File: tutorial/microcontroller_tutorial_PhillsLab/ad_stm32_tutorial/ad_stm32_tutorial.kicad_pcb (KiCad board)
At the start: 2 copper layers, 41 x 25.8 mm, 34 parts, among them J1 USB_C_Receptacle_USB2.0_16P, J2 TagConnect_TC2030-NL, J3 Conn_01x06, U1 STM32F042G6Ux, Y1 Crystal_GND24

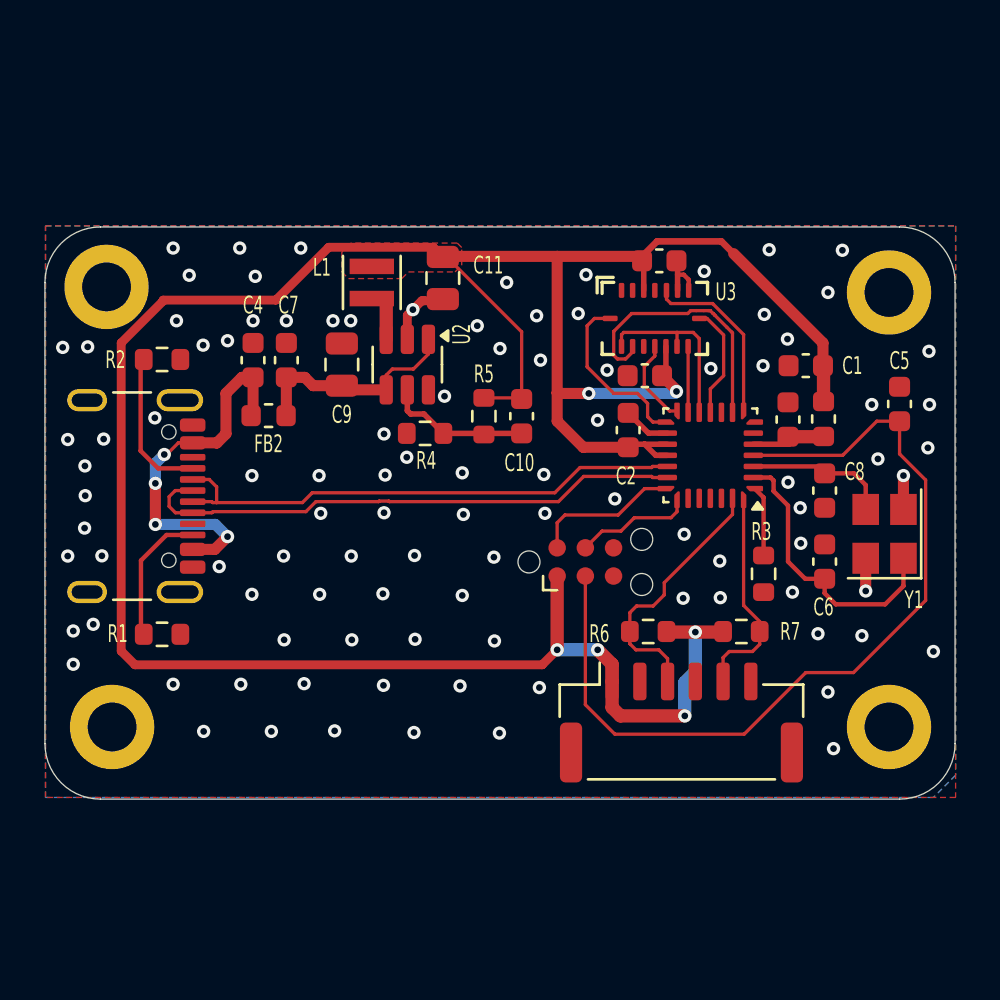
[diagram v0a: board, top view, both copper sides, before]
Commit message: Added all 3d models
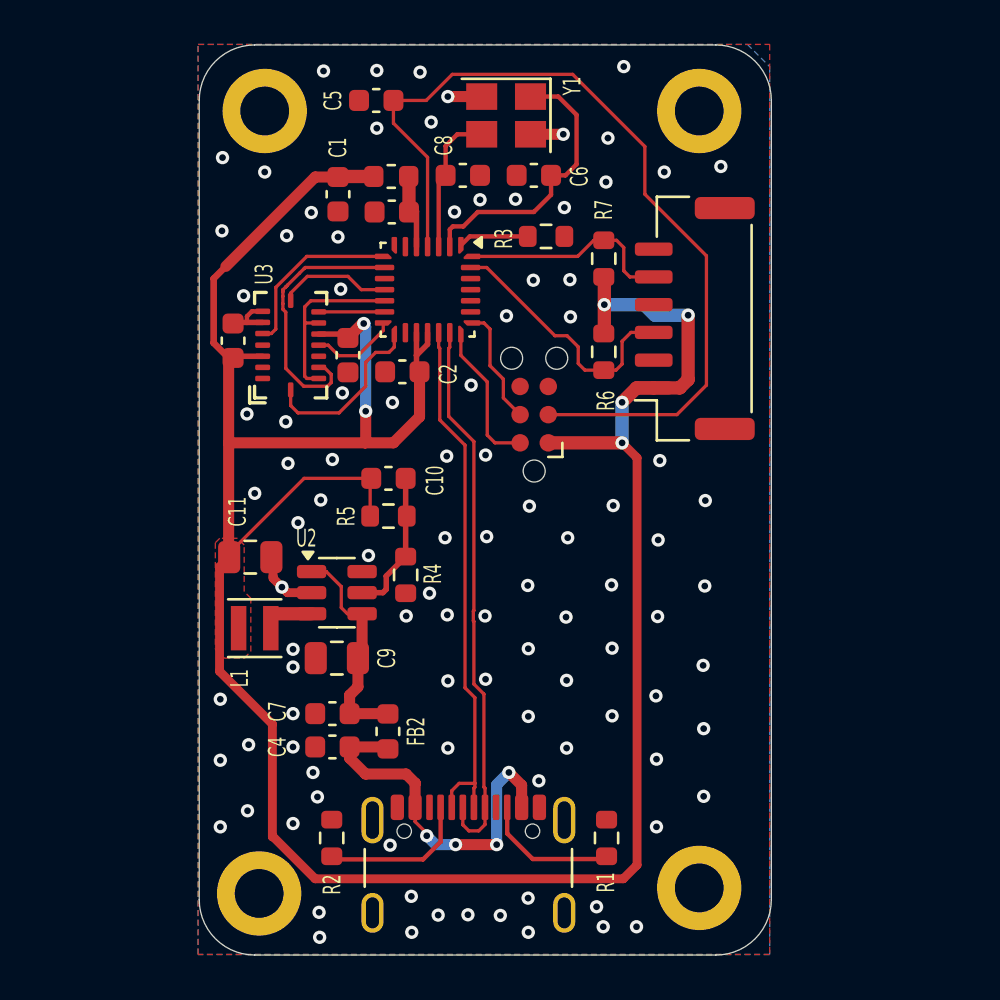
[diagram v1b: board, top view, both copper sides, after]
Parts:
- moved REF** 29.3 mm to (129.1, 70.6), turned to 90 degrees
- moved REF** 29.0 mm to (148.7, 70.6), turned to 90 degrees
- moved REF** 28.2 mm to (128.9, 105.8), turned to 90 degrees
- moved REF** 27.4 mm to (148.7, 105.6), turned to 90 degrees
- moved C5 27.3 mm to (134.2, 70.1), turned to 180 degrees
- moved Y1 25.4 mm to (140.0, 70.8), turned to 180 degrees
- moved J1 23.9 mm to (138.3, 105.6), turned to 0 degrees
- moved R2 22.9 mm to (132.1, 103.3), turned to 90 degrees
- moved C1 22.4 mm to (132.4, 74.3), turned to -90 degrees
- moved FB1 22.3 mm to (134.8, 73.5), turned to 0 degrees
- moved R1 22.0 mm to (144.5, 103.3), turned to 90 degrees
- moved C6 21.8 mm to (141.2, 73.5), turned to 180 degrees
- moved C8 21.6 mm to (138.1, 73.5), turned to 0 degrees
- moved C3 20.2 mm to (134.8, 75.1), turned to 180 degrees
- moved C12 19.5 mm to (127.7, 80.9), turned to 90 degrees
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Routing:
- net GND: track 10.7 -> 8.54 mm
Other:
- board size 41 x 25.8 mm -> 25.8 x 41 mm
